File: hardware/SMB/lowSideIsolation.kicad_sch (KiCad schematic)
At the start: 10 parts

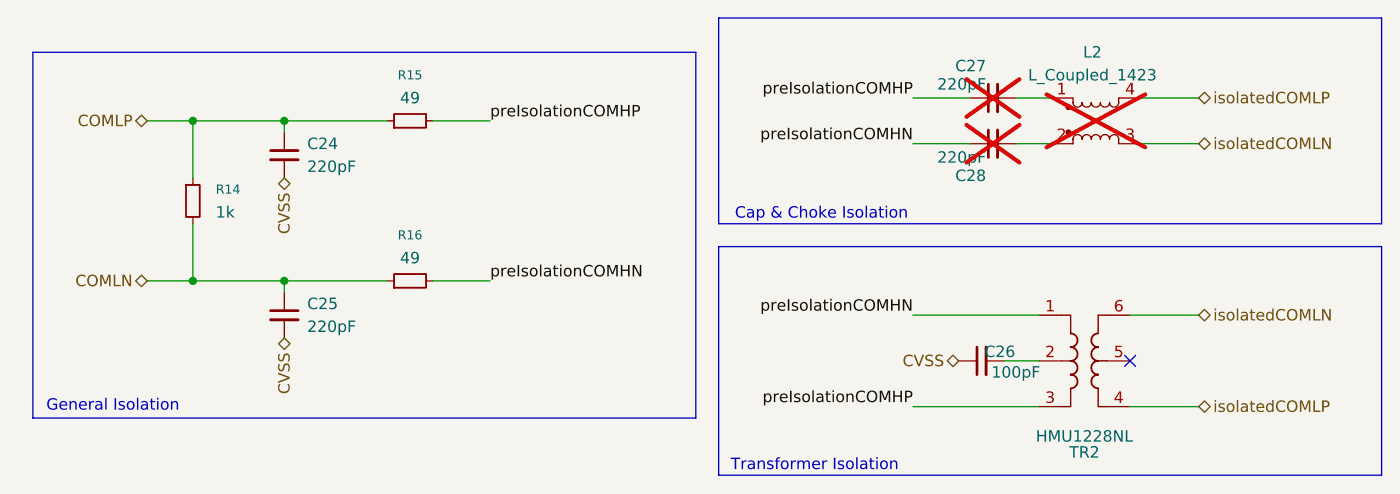
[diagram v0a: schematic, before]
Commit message: added BOM
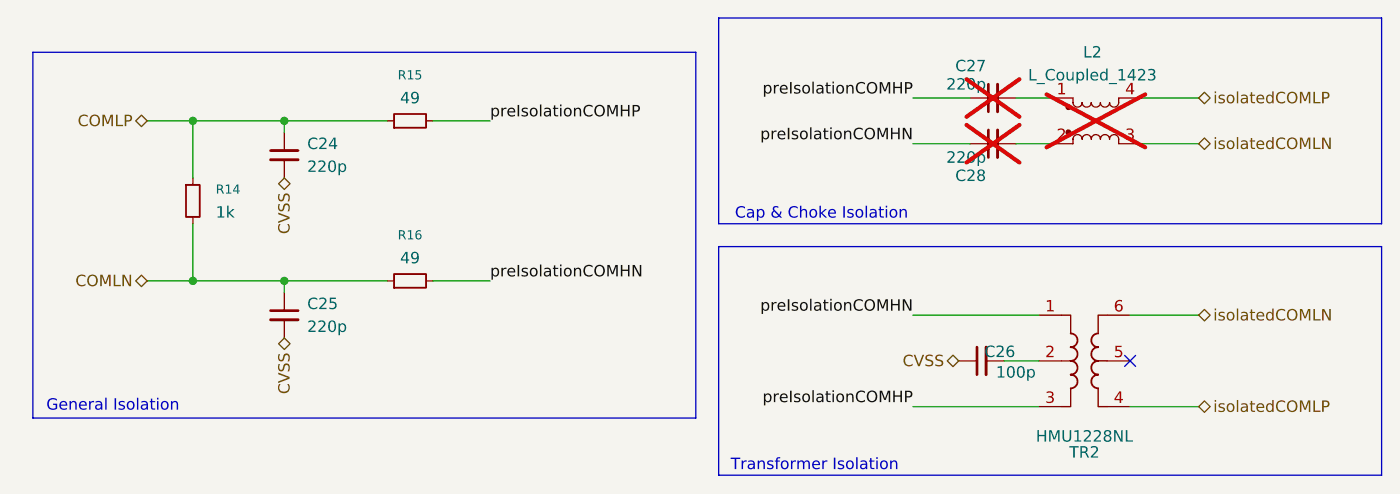
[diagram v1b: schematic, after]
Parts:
- C24, C25, C27, C28: value 220pF -> 220p; P/N (none) -> CC0603JRNPO9BN221
- C26: value 100pF -> 100p; P/N (none) -> KGM15AR71C101KT
- L2: P/N (none) -> 744242471
- R14: P/N (none) -> 0603WAF1001T5E
- R15, R16: P/N (none) -> RC0603FR-0749R9L
- TR2: P/N (none) -> HMU1228NL
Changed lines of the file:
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@@
+			)
+		)
+		(property "P/N" "744242471"
+			(at 185.42 93.98 0)
+			(hide yes)
+			(show_name no)
+			(do_not_autoplace no)
+			(effects
+				(font
+					(size 1.27 1.27)
+				)
 			)
 		)
@@
 			)
 		)
-		(property "Value" "100pF"
+		(property "Value" "100p"
 			(at 176.53 121.92 90)
 			(show_name no)
@@
 		(property "Description" "Unpolarized capacitor, small symbol"
 			(at 172.72 120.65 0)
+			(hide yes)
+			(show_name no)
+			(do_not_autoplace no)
+			(effects
+				(font
+					(size 1.27 1.27)
+				)
+			)
+		)
+		(property "P/N" "KGM15AR71C101KT"
+			(at 172.72 120.65 90)
 			(hide yes)
 			(show_name no)
@@
 			)
 		)
-		(property "Value" "220pF"
+		(property "Value" "220p"
 			(at 173.228 98.044 90)
 			(show_name no)
@@
 		(property "Description" "Unpolarized capacitor, small symbol"
 			(at 173.99 96.52 0)
+			(hide yes)
+			(show_name no)
+			(do_not_autoplace no)
+			(effects
+				(font
+					(size 1.27 1.27)
+				)
+			)
+		)
+		(property "P/N" "CC0603JRNPO9BN221"
+			(at 173.99 96.52 90)
 			(hide yes)
 			(show_name no)
@@
 			)
 		)
-		(property "Value" "220pF"
+		(property "Value" "220p"
 			(at 173.228 89.916 90)
 			(show_name no)
@@
 		(property "Description" "Unpolarized capacitor, small symbol"
 			(at 173.99 91.44 0)
+			(hide yes)
+			(show_name no)
+			(do_not_autoplace no)
+			(effects
+				(font
+					(size 1.27 1.27)
+				)
+			)
+		)
+		(property "P/N" "CC0603JRNPO9BN221"
+			(at 173.99 91.44 90)
 			(hide yes)
 			(show_name no)
@@
 			)
 		)
+		(property "P/N" "RC0603FR-0749R9L"
+			(at 109.22 111.76 90)
+			(hide yes)
+			(show_name no)
+			(do_not_autoplace no)
+			(effects
+				(font
+					(size 1.27 1.27)
+				)
+			)
+		)
 		(pin "1"
 		)
@@
 			)
 		)
-		(property "Value" "220pF"
+		(property "Value" "220p"
 			(at 97.79 116.8462 0)
 			(show_name no)
@@
 		)
 		(property "Description" "Unpolarized capacitor, small symbol"
+			(at 95.25 115.57 0)
+			(hide yes)
+			(show_name no)
+			(do_not_autoplace no)
+			(effects
+				(font
+					(size 1.27 1.27)
+				)
+			)
+		)
+		(property "P/N" "CC0603JRNPO9BN221"
 			(at 95.25 115.57 0)
 			(hide yes)
@@
 			)
 		)
+		(property "P/N" "RC0603FR-0749R9L"
+			(at 109.22 93.98 90)
+			(hide yes)
+			(show_name no)
+			(do_not_autoplace no)
+			(effects
+				(font
+					(size 1.27 1.27)
+				)
+			)
+		)
 		(pin "1"
 		)
@@
 			)
 		)
+		(property "P/N" "0603WAF1001T5E"
+			(at 85.09 102.87 0)
+			(hide yes)
+			(show_name no)
+			(do_not_autoplace no)
+			(effects
+				(font
+					(size 1.27 1.27)
+				)
+			)
+		)
 		(pin "1"
 		)
@@
 			)
 		)
+		(property "P/N" "HMU1228NL"
+			(at 184.15 120.65 0)
+			(hide yes)
+			(show_name no)
+			(do_not_autoplace no)
+			(effects
+				(font
+					(size 1.27 1.27)
+				)
+			)
+		)
 		(pin "4"
 		)
@@
 			)
 		)
-		(property "Value" "220pF"
+		(property "Value" "220p"
 			(at 97.79 99.0662 0)
 			(show_name no)
@@
 			(at 95.25 97.79 0)
 			(hide yes)
+			(show_name no)
+			(do_not_autoplace no)
+			(effects
+				(font
+					(size 1.27 1.27)
+				)
+			)
+		)
+		(property "P/N" "CC0603JRNPO9BN221"
+			(at 95.25 97.79 0)
+			(hide yes)
